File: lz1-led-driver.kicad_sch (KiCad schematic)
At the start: 2 parts

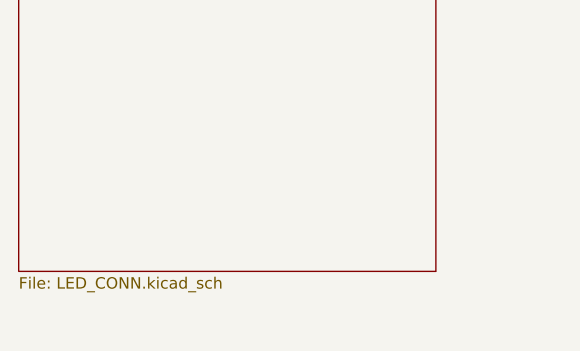
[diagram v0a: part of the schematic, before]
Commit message: Update naming convention
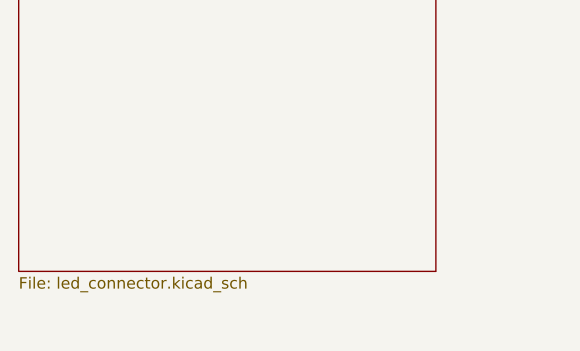
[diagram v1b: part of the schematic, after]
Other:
- sheet LEDS & CONNECTORS: file LED_CONN.kicad_sch -> led_connector.kicad_sch
- title: 1050nm IR LED Driver -> LZ1 OSRAM LuxiGen LED Driver
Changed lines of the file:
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@@
   (paper "A3")
   (title_block
-    (title "1050nm IR LED Driver")
-    (date "2023-04-14")
+    (title "LZ1 OSRAM LuxiGen LED Driver")
+    (date "2023-05-04")
     (rev "1.0.0")
     (company "Antmicro Ltd.")
@@
       (effects (font (size 1.27 1.27)) (justify left bottom))
     )
-    (property "Sheet file" "LED_CONN.kicad_sch" (id 1) (at 131.445 236.8046 0)
+    (property "Sheet file" "led_connector.kicad_sch" (id 1) (at 131.445 236.8046 0)
       (effects (font (size 1.27 1.27)) (justify left top))
     )
@@
       (reference "#PWR0101") (unit 1) (value "GND") (footprint "")
     )
+    (path "/02863aa0-7d3f-4a49-bbc3-667fd8cc786e/25c8adc3-90d0-416c-a094-61de9297b643"
+      (reference "#PWR?") (unit 1) (value "GND") (footprint "")
+    )
     (path "/02863aa0-7d3f-4a49-bbc3-667fd8cc786e/445201a1-fca5-4fa3-a943-a4c42d093c71"
-      (reference "#PWR0102") (unit 1) (value "GND") (footprint "")
-    )
-    (path "/02863aa0-7d3f-4a49-bbc3-667fd8cc786e/25c8adc3-90d0-416c-a094-61de9297b643"
-      (reference "#PWR0103") (unit 1) (value "GND") (footprint "")
+      (reference "#PWR?") (unit 1) (value "GND") (footprint "")
     )
     (path "/04f57430-8668-4227-a3f5-414daa4e8985/db0ab990-568d-4a92-bc6c-ab27d31f5e7a"

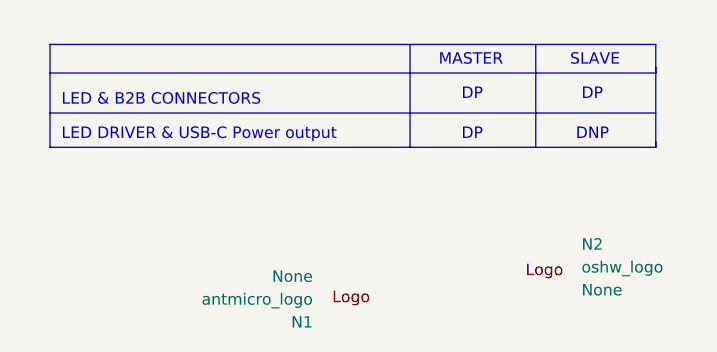
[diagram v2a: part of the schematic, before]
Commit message: Correct sch logos. Update PCB from schematic
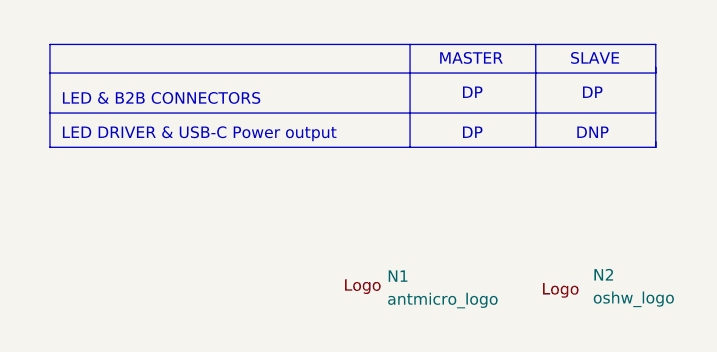
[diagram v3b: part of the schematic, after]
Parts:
- N1, N2: Author (none) -> Antmicro; Copyright Copyright (c) 2023 Antmicro -> (none); License Apache-2.0 License -> Apache-2.0; Manufacturer None -> (none)
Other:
- moved on the sheet: N1, N2
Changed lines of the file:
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@@
     (effects (font (size 1.27 1.27)) (justify left bottom))
   )
-  (symbol (lib_id "antmicroMechanicalParts:oshw_logo") (at 365.125 235.585 0) (unit 1)
+  (symbol (lib_id "antmicroMechanicalParts:oshw_logo") (at 367.665 238.76 0) (unit 1)
     (in_bom yes) (on_board yes) (fields_autoplaced)
-    (property "Reference" "N2" (id 0) (at 372.11 233.0385 0)
+    (property "Reference" "N2" (id 0) (at 373.38 236.4675 0)
       (effects (font (size 1.27 1.27) (thickness 0.15)) (justify left))
     )
-    (property "Value" "oshw_logo" (id 1) (at 372.11 235.5785 0)
+    (property "Value" "oshw_logo" (id 1) (at 373.38 239.0075 0)
       (effects (font (size 1.27 1.27) (thickness 0.15)) (justify left))
     )
-    (property "Footprint" "antmicro-footprints:oshw-logo" (id 2) (at 380.365 245.745 0)
+    (property "Footprint" "antmicro-footprints:oshw-logo" (id 2) (at 382.905 248.92 0)
       (effects (font (size 1.27 1.27) (thickness 0.15)) (justify left bottom) hide)
     )
-    (property "Datasheet" "" (id 3) (at 380.365 248.285 0)
+    (property "Datasheet" "" (id 3) (at 382.905 251.46 0)
       (effects (font (size 1.27 1.27) (thickness 0.15)) (justify left bottom) hide)
     )
-    (property "Copyright" "Copyright (c) 2023 Antmicro" (id 4) (at 380.365 250.825 0)
+    (property "License" "Apache-2.0" (id 5) (at 382.905 256.54 0)
       (effects (font (size 1.27 1.27) (thickness 0.15)) (justify left bottom) hide)
     )
-    (property "License" "Apache-2.0 License" (id 5) (at 380.365 253.365 0)
+    (property "Manufacturer" "" (id 6) (at 382.905 259.08 0)
       (effects (font (size 1.27 1.27) (thickness 0.15)) (justify left bottom) hide)
     )
-    (property "Manufacturer" "None" (id 6) (at 372.11 238.1185 0)
-      (effects (font (size 1.27 1.27)) (justify left))
+    (property "Author" "Antmicro" (id 7) (at 382.905 254 0)
+      (effects (font (size 1.27 1.27) (thickness 0.15)) (justify left bottom) hide)
+    )
+    (property "MPN" "" (id 7) (at 367.665 238.76 0)
+      (effects (font (size 1.27 1.27)) hide)
     )
   )
   (symbol (lib_id "antmicroMechanicalParts:antmicro_logo") (at 349.885 236.855 180) (unit 1)
     (in_bom yes) (on_board yes) (fields_autoplaced)
-    (property "Reference" "N1" (id 0) (at 342.265 241.6875 0)
-      (effects (font (size 1.27 1.27) (thickness 0.15)) (justify left))
+    (property "Reference" "N1" (id 0) (at 350.52 236.6072 0)
+      (effects (font (size 1.27 1.27) (thickness 0.15)) (justify right))
     )
-    (property "Value" "antmicro_logo" (id 1) (at 342.265 239.1475 0)
-      (effects (font (size 1.27 1.27) (thickness 0.15)) (justify left))
+    (property "Value" "antmicro_logo" (id 1) (at 350.52 239.1472 0)
+      (effects (font (size 1.27 1.27) (thickness 0.15)) (justify right))
     )
     (property "Footprint" "antmicro-footprints:antmicro-logo_scaled_12mm" (id 2) (at 334.645 226.695 0)
@@
       (effects (font (size 1.27 1.27) (thickness 0.15)) (justify left bottom) hide)
     )
-    (property "Copyright" "Copyright (c) 2023 Antmicro" (id 4) (at 334.645 221.615 0)
+    (property "License" "Apache-2.0" (id 5) (at 334.645 219.075 0)
       (effects (font (size 1.27 1.27) (thickness 0.15)) (justify left bottom) hide)
     )
-    (property "License" "Apache-2.0 License" (id 5) (at 334.645 219.075 0)
+    (property "Manufacturer" "" (id 6) (at 334.645 216.535 0)
       (effects (font (size 1.27 1.27) (thickness 0.15)) (justify left bottom) hide)
     )
-    (property "Manufacturer" "None" (id 6) (at 342.265 236.6075 0)
-      (effects (font (size 1.27 1.27)) (justify left))
+    (property "MPN" "" (id 7) (at 349.885 236.855 0)
+      (effects (font (size 1.27 1.27)) hide)
+    )
+    (property "Author" "Antmicro" (id 7) (at 334.645 221.615 0)
+      (effects (font (size 1.27 1.27) (thickness 0.15)) (justify left bottom) hide)
     )
   )
@@
     )
     (path "/02863aa0-7d3f-4a49-bbc3-667fd8cc786e/25c8adc3-90d0-416c-a094-61de9297b643"
-      (reference "#PWR?") (unit 1) (value "GND") (footprint "")
+      (reference "#PWR0102") (unit 1) (value "GND") (footprint "")
     )
     (path "/02863aa0-7d3f-4a49-bbc3-667fd8cc786e/445201a1-fca5-4fa3-a943-a4c42d093c71"
-      (reference "#PWR?") (unit 1) (value "GND") (footprint "")
+      (reference "#PWR0103") (unit 1) (value "GND") (footprint "")
     )
     (path "/04f57430-8668-4227-a3f5-414daa4e8985/db0ab990-568d-4a92-bc6c-ab27d31f5e7a"

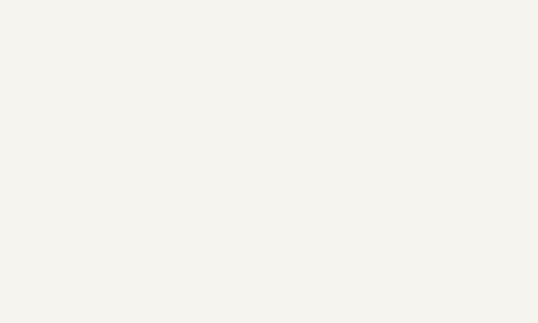
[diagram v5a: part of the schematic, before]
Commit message: Introduced schematic standardization
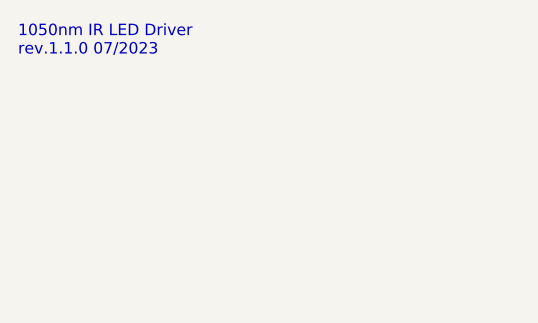
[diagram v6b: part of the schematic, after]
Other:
- note added: "1050nm IR LED Driver rev.${REVISION} 07/2023"
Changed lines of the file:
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@@
+    (effects (font (size 1.27 1.27)) (justify left bottom))
+  )
+  (text "1050nm IR LED Driver \nrev.${REVISION} 07/2023" (at 116.84 -6.35 0)
     (effects (font (size 1.27 1.27)) (justify left bottom))
   )
@@
       (reference "#PWR01") (unit 1) (value "+12V") (footprint "")
     )
-    (path "/04f57430-8668-4227-a3f5-414daa4e8985/ef8beb8d-279c-420e-82ac-ed93404580bd"
-      (reference "#PWR02") (unit 1) (value "GND") (footprint "")
-    )
     (path "/04f57430-8668-4227-a3f5-414daa4e8985/3dfd95ab-8c8e-4d0d-bb2d-5eda20546d8f"
       (reference "#PWR03") (unit 1) (value "+12V") (footprint "")
@@
       (reference "#PWR0106") (unit 1) (value "GND") (footprint "")
     )
+    (path "/02863aa0-7d3f-4a49-bbc3-667fd8cc786e/2667207a-8dab-41ba-aa7f-d8203e45b043"
+      (reference "#PWR0107") (unit 1) (value "GND") (footprint "")
+    )
+    (path "/02863aa0-7d3f-4a49-bbc3-667fd8cc786e/22c680c0-3b3a-46bb-ac02-93e78527c47f"
+      (reference "#PWR0108") (unit 1) (value "GND") (footprint "")
+    )
+    (path "/04f57430-8668-4227-a3f5-414daa4e8985/8ebb2fba-93d6-43aa-a42e-d17596005075"
+      (reference "#PWR0109") (unit 1) (value "GND") (footprint "")
+    )
+    (path "/04f57430-8668-4227-a3f5-414daa4e8985/16f44e5f-c530-4a99-9833-cb6c56d8b386"
+      (reference "#PWR0110") (unit 1) (value "GND") (footprint "")
+    )
     (path "/04f57430-8668-4227-a3f5-414daa4e8985/db0ab990-568d-4a92-bc6c-ab27d31f5e7a"
-      (reference "C1") (unit 1) (value "C_10u_0805") (footprint "antmicro-footprints:0805-cap")
+      (reference "C1") (unit 1) (value "C_10u_0805") (footprint "antmicro-footprints:C_0805_2012Metric")
     )
     (path "/04f57430-8668-4227-a3f5-414daa4e8985/b52a5a90-7ff7-4a99-b275-e56c92499b83"
@@
     )
     (path "/04f57430-8668-4227-a3f5-414daa4e8985/18101bec-567a-48ba-b51c-27aef041db15"
-      (reference "J2") (unit 1) (value "USB-C_USB4105-GF-A") (footprint "antmicro-footprints:GCT_USB4105-GF-A")
+      (reference "J2") (unit 1) (value "USB-C_USB4105-GF-A") (footprint "antmicro-footprints:USB-C_GCT_USB4105-GF-A")
     )
     (path "/02863aa0-7d3f-4a49-bbc3-667fd8cc786e/34a6d581-d7e5-4631-99ef-5078a62bade8"
@@
       (reference "J4") (unit 1) (value "SM02B-SRSS-TB-LF-SN") (footprint "antmicro-footprints:JST_SM02B-SRSS-TB-LF-SN")
     )
-    (path "/04f57430-8668-4227-a3f5-414daa4e8985/654307fb-8bf3-40f6-9634-02b9debd8418"
-      (reference "L1") (unit 1) (value "SRP2512A-4R7M") (footprint "antmicro-footprints:SRP2512A-1R0M")
+    (path "/04f57430-8668-4227-a3f5-414daa4e8985/20bbbcf9-5a9c-4550-9025-4e5ba4235f41"
+      (reference "L1") (unit 1) (value "L_4u7_1.5A_1008") (footprint "antmicro-footprints:SRP2512A-1R0M")
     )
     (path "/04f57430-8668-4227-a3f5-414daa4e8985/c9d38ffe-3b5e-4711-87e6-b88239efe34c"
@@
       (reference "U1") (unit 1) (value "MP2483DQ-LF-P") (footprint "antmicro-footprints:QFN-10-1EP_3x3mm_P0.5mm")
     )
-    (path "/04f57430-8668-4227-a3f5-414daa4e8985/3d030c89-fe83-45b7-bbf9-701f0bf5b12e"
+    (path "/04f57430-8668-4227-a3f5-414daa4e8985/7a3e6d9f-32ba-467e-9dc7-da6afd2bd33b"
       (reference "U2") (unit 1) (value "AP62301Z6-7") (footprint "antmicro-footprints:SOT-563")
     )

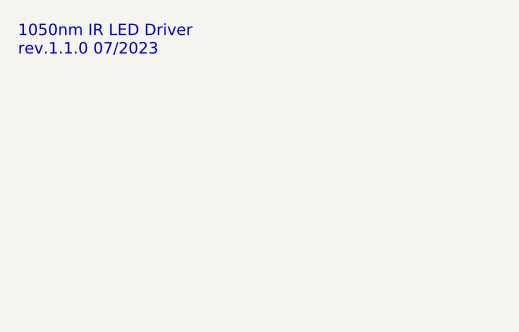
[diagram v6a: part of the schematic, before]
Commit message: [50954] Added CC resistors and OHP assets, updated README
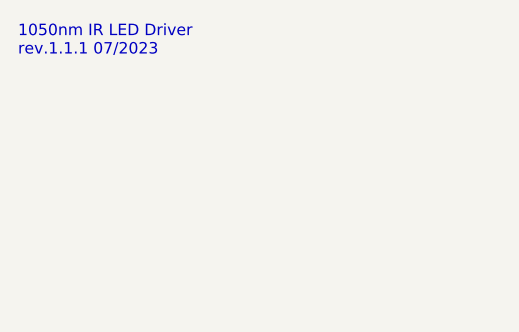
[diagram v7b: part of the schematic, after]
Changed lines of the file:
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@@
   (title_block
     (title "LZ1 OSRAM LuxiGen LED Driver")
-    (date "2023-05-04")
-    (rev "1.1.0")
+    (date "2023-11-03")
+    (rev "1.1.1")
     (company "Antmicro Ltd.")
     (comment 1 "www.antmicro.com")
@@
       (reference "J1") (unit 1) (value "BarrelJack_3167288") (footprint "antmicro-footprints:BarrelJack_3167288_Horizontal")
     )
-    (path "/04f57430-8668-4227-a3f5-414daa4e8985/18101bec-567a-48ba-b51c-27aef041db15"
-      (reference "J2") (unit 1) (value "USB-C_USB4105-GF-A") (footprint "antmicro-footprints:USB-C_GCT_USB4105-GF-A")
-    )
-    (path "/02863aa0-7d3f-4a49-bbc3-667fd8cc786e/34a6d581-d7e5-4631-99ef-5078a62bade8"
-      (reference "J3") (unit 1) (value "SM02B-SRSS-TB-LF-SN") (footprint "antmicro-footprints:JST_SM02B-SRSS-TB-LF-SN")
-    )
-    (path "/02863aa0-7d3f-4a49-bbc3-667fd8cc786e/c443b677-61e8-4896-8031-467e4fb3fc90"
-      (reference "J4") (unit 1) (value "SM02B-SRSS-TB-LF-SN") (footprint "antmicro-footprints:JST_SM02B-SRSS-TB-LF-SN")
+    (path "/04f57430-8668-4227-a3f5-414daa4e8985/60cd8ca0-56eb-4f96-bdaa-e86beaa72421"
+      (reference "J2") (unit 1) (value "USB-C_GCT_USB4105-GF-A") (footprint "antmicro-footprints:USB-C_Receptacle_GCT_USB4105-GF-A")
+    )
+    (path "/02863aa0-7d3f-4a49-bbc3-667fd8cc786e/94f39941-f2dd-4511-a5e7-553b03038b2b"
+      (reference "J3") (unit 1) (value "JST_SH_1x2_SM02B-SRSS-TB-LF-SN") (footprint "antmicro-footprints:Conn_JST_SH_1x2_SM02B-SRSS-TB-LF-SN")
+    )
+    (path "/02863aa0-7d3f-4a49-bbc3-667fd8cc786e/084b9e67-b8c5-41ec-a18f-406c6d540687"
+      (reference "J4") (unit 1) (value "JST_SH_1x2_SM02B-SRSS-TB-LF-SN") (footprint "antmicro-footprints:Conn_JST_SH_1x2_SM02B-SRSS-TB-LF-SN")
     )
     (path "/04f57430-8668-4227-a3f5-414daa4e8985/20bbbcf9-5a9c-4550-9025-4e5ba4235f41"
@@
       (reference "R14") (unit 1) (value "R_10k_0402") (footprint "antmicro-footprints:R_0402_1005Metric")
     )
+    (path "/04f57430-8668-4227-a3f5-414daa4e8985/c986fbf4-4948-4743-b44b-94032e925a79"
+      (reference "R15") (unit 1) (value "R_22k_0402") (footprint "antmicro-footprints:R_0402_1005Metric")
+    )
+    (path "/04f57430-8668-4227-a3f5-414daa4e8985/f00099d8-e1e8-4826-a986-c2132aaa3e9b"
+      (reference "R16") (unit 1) (value "R_22k_0402") (footprint "antmicro-footprints:R_0402_1005Metric")
+    )
     (path "/04f57430-8668-4227-a3f5-414daa4e8985/88771d0b-247a-456b-8199-2d4dafeaa2a0"
